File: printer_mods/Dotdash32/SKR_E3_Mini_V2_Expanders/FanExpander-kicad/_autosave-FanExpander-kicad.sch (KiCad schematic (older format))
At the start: 65 parts, among them J0 FAN0, J1 FAN1, J10 FAN0_IN, J11 HI_PWR_IN, J2 FAN2, J3 FAN3, J4 FAN4, J5 FAN5, J6 FAN6, J7 FAN7, J8 EXP1_IN, J9 5V_In, Q1 IRLML6344, Q2 IRLML6344, Q3 IRLML6344, Q4 IRLML6344, Q5 IRLML6344, Q6 IRLML6344, Q7 IRLML6344

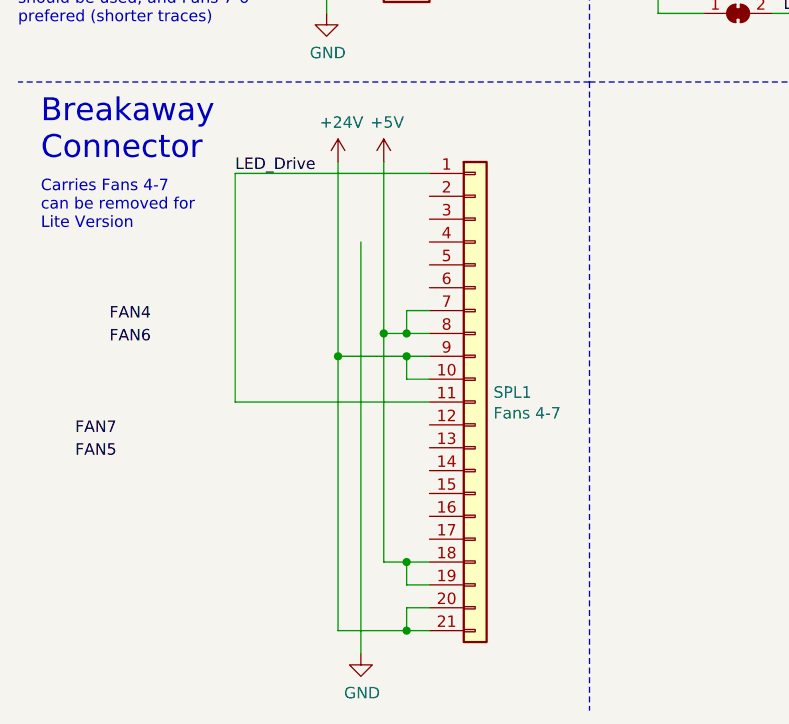
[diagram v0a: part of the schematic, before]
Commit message: chore: trying routing, running into obstacles
no room to route the control wires, everything else is *almost*
there though.
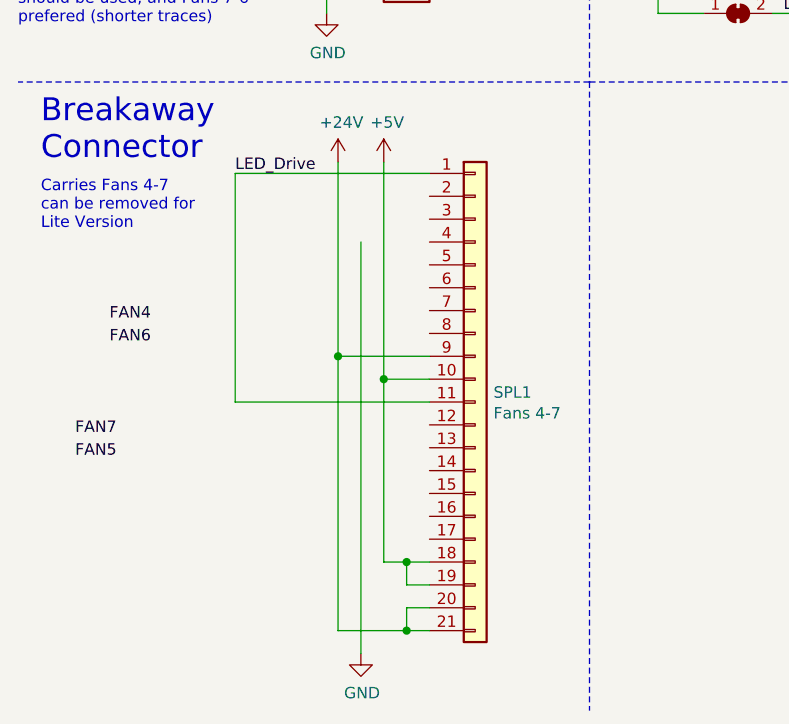
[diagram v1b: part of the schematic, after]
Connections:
- net +24V: no longer SPL1.10 (Pin_10)
- net +5V: now also SPL1.10 (Pin_10); no longer SPL1.7 (Pin_7), SPL1.8 (Pin_8)
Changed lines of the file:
@@
 $EndComp
-Wire Wire Line
-	2100 5600 2100 6350
 Wire Wire Line
 	2300 7350 2200 7350
@@
 	1450 5650 1450 6650
 Wire Wire Line
-	2300 6450 2200 6450
-Wire Wire Line
-	2300 6550 2200 6550
-Wire Wire Line
-	2200 6550 2200 6450
-Wire Wire Line
-	2300 6350 2200 6350
-Wire Wire Line
-	2300 6250 2200 6250
-Wire Wire Line
-	2200 6250 2200 6350
-Connection ~ 2200 6350
-Wire Wire Line
-	2200 6350 2100 6350
-Connection ~ 2100 6350
+	2100 5600 2100 6550
 Wire Wire Line
 	1900 5600 1900 6450
 Wire Wire Line
-	2100 6350 2100 7350
+	2300 6550 2100 6550
+Connection ~ 2100 6550
 Wire Wire Line
-	2200 6450 1900 6450
-Connection ~ 2200 6450
+	2100 6550 2100 7350
+Wire Wire Line
+	2300 6450 1900 6450
 Connection ~ 1900 6450
 Wire Wire Line
